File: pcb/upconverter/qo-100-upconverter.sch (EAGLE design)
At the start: 222 parts, among them CON1 3P-SH-SIDE, CON2 2EDG-2P-5MM-H, U1 EFM32TG11B120F128GM32, U10 LTC5597, U11 2450BP15E0100, U12 DC2337J5010AHF, U13 MCP6V31, U14 SKY66292-11, U15 F1958NBGK, U16 MCP9802-A0, U17 MCP1700-330, U18 LT8636, U19 MCP3421-A0, U2 DSB321SDA, U20 MCP6C02-020, U21 ADP7142AUJZ-3.3, U22 ADP7142AUJZ-3.3, U23 ADP7142AUJZ-3.3, U24 ADM7171ACPZ-5.0, U25 ADM7172ACPZ-5.0, U3 ADF4351, U4 F1958NBGK, U5 MAX2671, U6 2450BP15E0100, U7 F1958NBGK, U8 ADL5601, U9 F1490NLGA

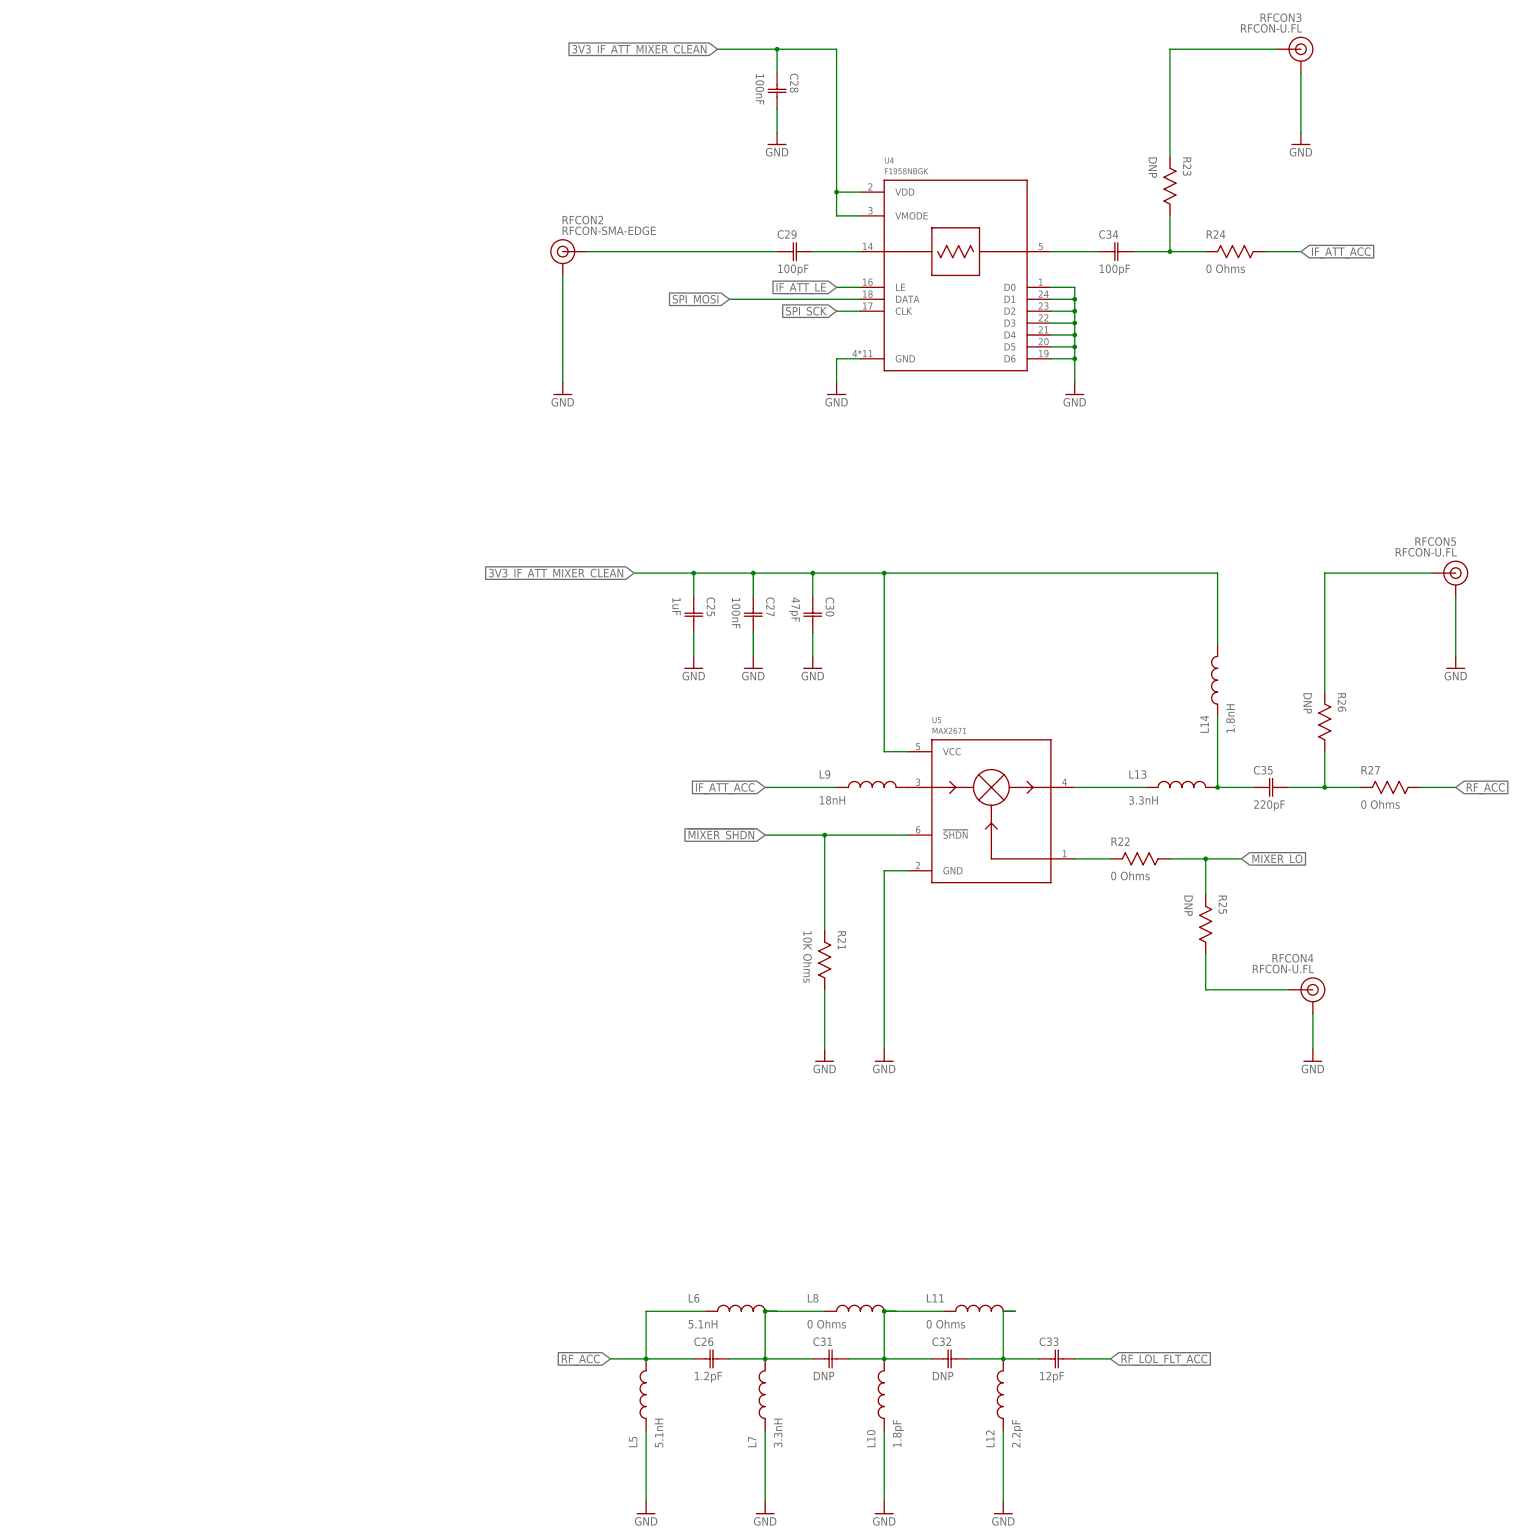
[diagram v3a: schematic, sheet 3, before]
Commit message: Add RF switch
Signed-off-by: João Silva <jgc3silva@gmail.com>
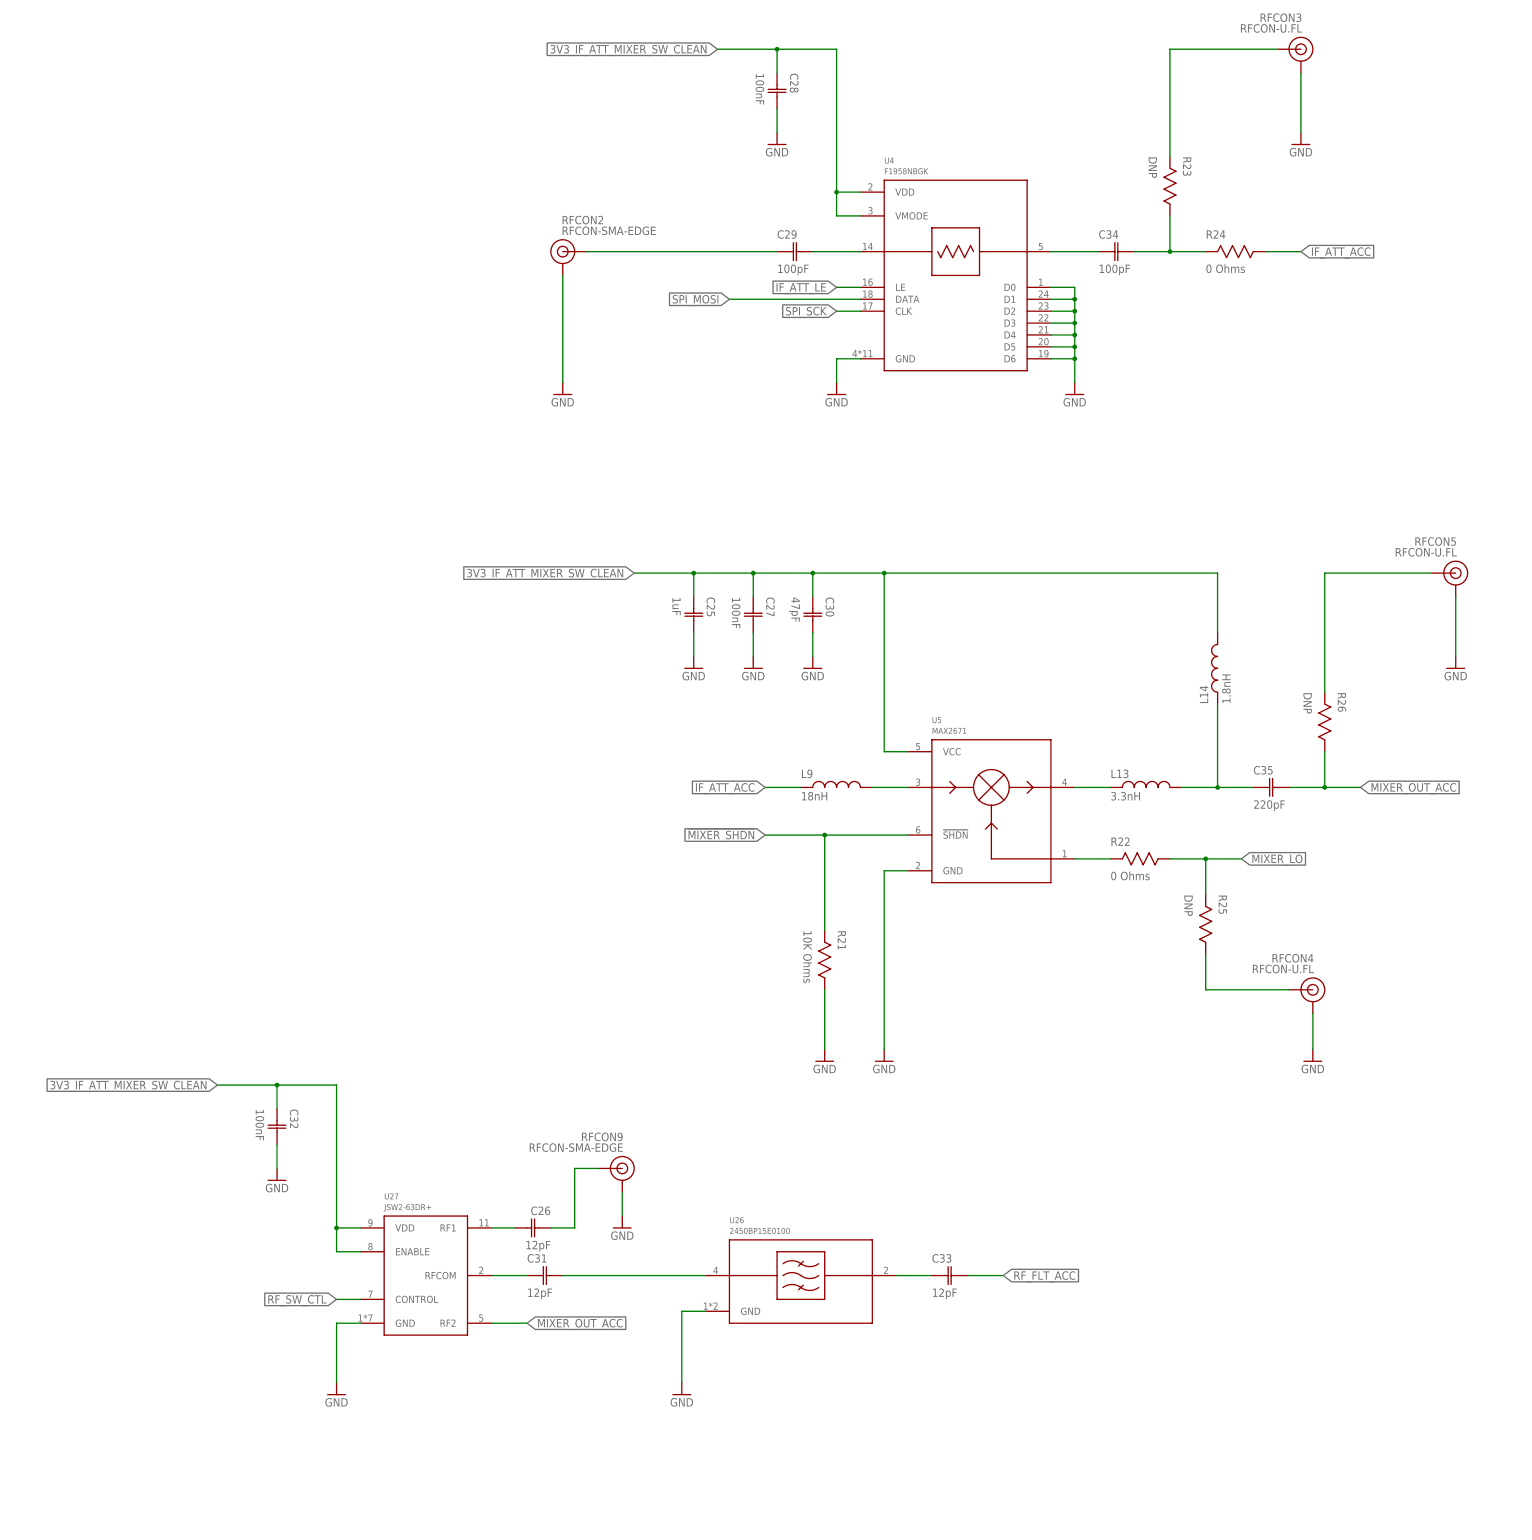
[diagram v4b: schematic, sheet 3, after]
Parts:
- removed L10: 1.8pF, Inductor:INDUCTOR-0603
- removed L11, L8: 0 Ohms, Inductor:INDUCTOR-0603
- removed L12: 2.2pF, Inductor:INDUCTOR-0603
- removed L5, L6: 5.1nH, Inductor:INDUCTOR-0603
- removed L7: 3.3nH, Inductor:INDUCTOR-0603
- removed R27: 0 Ohms, Resistor:RESISTOR-0603
- added RFCON9: RFCON-SMA-EDGE, RF Connector:RFCON-SMA-EDGE
- added U26: 2450BP15E0100, Generic Filter:2450BP15E0100
- added U27: JSW2-63DR+, Mini Circuits:JSW2-63DR+
- C26: value 1.2pF -> 12pF
- C31: value DNP -> 12pF
- C32: value DNP -> 100nF
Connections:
- net RF_LOL_FLT_ACC renamed RF_FLT_ACC
- removed net 3V3_IF_ATT_MIXER_CLEAN: C25.C1, C27.C1, C28.C1, C30.C1, C93.C1, L14.2, U21.SENSE/ADJ, U21.VOUT, U4.VDD, U4.VMODE, U5.VCC
- removed net MIXER_OUT_ACC_PROBE: C35.C2, R26.1, R27.2
- removed net N$32: C26.C2, C31.C1, L6.2, L7.2, L8.1
- removed net N$33: C31.C2, C32.C1, L10.2, L11.1, L8.2
- removed net N$34: C32.C2, C33.C1, L11.2, L12.2
- removed net RF_ACC: C26.C1, L5.2, L6.1, R27.1
- new net 3V3_IF_ATT_MIXER_SW_CLEAN: C25.C1, C27.C1, C28.C1, C30.C1, C32.C1, C93.C1, L14.2, U21.SENSE/ADJ, U21.VOUT, U27.ENABLE, U27.VDD, U4.VDD, U4.VMODE, U5.VCC
- new net MIXER_OUT_ACC: C35.C2, R26.1, U27.RF2
- new net RF_IN_ACC: C26.C2, U27.RF1
- new net RF_IN_DCC: C26.C1, RFCON9.SIGNAL
- new net RF_SEL_ACC: C31.C2, U26.RFIN
- new net RF_SEL_DCC: C31.C1, U27.RFCOM
- new net RF_SEL_FILT_DCC: C33.C1, U26.RFOUT
- new net RF_SW_CTL: U1.PC13, U27.CONTROL
- net GND: now also C32.C2, RFCON9.GND, U26.GND, U27.GND; no longer L10.1, L12.1, L5.1, L7.1
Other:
- moved on the sheet: C26, C31, C32, C33, L1, L13, L14, L15, L17, L2, L3, L4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

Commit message: Add Mixer and RF Switch indicator LEDs Slightly raise switched 5V0 rail voltage to account for larger current drawn from higher power last stage Remove dedicated ADC for current sampling Added PCB preview pictures Added schematic PDF
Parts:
- removed C81: 100nF, Capacitor:CAPACITOR-0603
- removed L16: 470nH, Inductor:INDUCTOR-0603
- removed R10: 100K Ohms, Resistor:RESISTOR-0603
- removed R52: 221K Ohms, Resistor:RESISTOR-0603
- removed RFCON9: RFCON-SMA-EDGE, RF Connector:RFCON-SMA-EDGE
- removed U21: ADP7142AUJZ-3.3, Analog Devices:ADP7142AUJZ-3.3
- added D7, D8: LED0603, LED:LED0603
- added L5: 18nH, Inductor:INDUCTOR-0603
- added R27: 1K Ohms, Resistor:RESISTOR-0603
- C25: value 1uF -> 100nF
- C26, C33: value 12pF -> 15pF
- C27: value 100nF -> 15pF
- C28: value 100nF -> 1uF
- C29: value 100pF -> 100nF
- C30: value 47pF -> 100nF
- C31: value 12pF -> 100pF
- C32: value 100nF -> 47pF
- C65: value 10nF -> 100nF
- C66, C77: value 100nF -> 10nF
- C67: value 15pF -> 100nF
- C68: value 4.7uF -> 15pF; VOLTAGE 35V -> (none)
- C69: value 100nF -> 4.7uF; VOLTAGE (none) -> 35V
- C70: value 470pF -> 100nF
- C72: value 4.7uF -> 470pF
- C73: value 1uF -> 4.7uF; VOLTAGE 50V -> (none)
- C75: VOLTAGE (none) -> 50V
- C76: value 10nF -> 1uF
- C78: value 10uF -> 100nF
- C80: value 100nF -> 10uF
- C82: value 10pF -> 100nF
- C83: value 1uF -> 10pF
- C84: value 100uF -> 1uF; device Capacitor:CAPACITOR-1206 -> Capacitor:CAPACITOR-0603
- C85: value 100nF -> 100uF; device Capacitor:CAPACITOR-0603 -> Capacitor:CAPACITOR-1206
- C87: value 22uF -> 100nF; device Capacitor:CAPACITOR-1206 -> Capacitor:CAPACITOR-0603
- C88: value 1uF -> 22uF; device Capacitor:CAPACITOR-0603 -> Capacitor:CAPACITOR-1206
- C93: value 10uF -> 1uF
- C96: value 1nF -> 10uF
- C98: value 10uF -> 1nF; device Capacitor:CAPACITOR-1206 -> Capacitor:CAPACITOR-0603; VOLTAGE 50V -> (none)
- C99: value 100nF -> 10uF; device Capacitor:CAPACITOR-0603 -> Capacitor:CAPACITOR-1206; VOLTAGE (none) -> 50V
- L9: value 18nH -> 470nH
- R28: value 1K Ohms -> DNP
- R30: value DNP -> 1.5K Ohms
- R31: value 1.5K Ohms -> 0 Ohms
- R32: value 0 Ohms -> 510 Ohms
- R33: value 510 Ohms -> 0 Ohms
- R34: value 0 Ohms -> 1K Ohms
- R35: value DNP -> 2K Ohms
- R36: value 1K Ohms -> 49.9 Ohms
- R37: value 2K Ohms -> 100 Ohms
- R38: value 49.9 Ohms -> 96.1 Ohms
- R39: value 100 Ohms -> 71.5 Ohms
- R41: value 71.5 Ohms -> 10K Ohms
- R42: value 96.1 Ohms -> 7.5K Ohms
- R43: value 10K Ohms -> 510 Ohms
- R44: value 7.5K Ohms -> 100K Ohms
- R45: value 510 Ohms -> 10K Ohms
- R47: value 10K Ohms -> 75K Ohms
- R48: value 100K Ohms -> 41.2K Ohms
- R49: value 75K Ohms -> 1M Ohms
- R50: value 41.2K Ohms -> 220K Ohms
- R51: value 1M Ohms -> 1K Ohms
- R53: value 10K Ohms -> 0.03 Ohms; device Resistor:RESISTOR-0603 -> Resistor:RESISTOR-1206; TOLERANCE (none) -> 1%
- R54: value 10K Ohms -> 100K Ohms
- R55: value 0.03 Ohms -> 100K Ohms; device Resistor:RESISTOR-1206 -> Resistor:RESISTOR-0603; TOLERANCE 1% -> (none)
- R56: value 100K Ohms -> 1K Ohms
- R57: value 100K Ohms -> 330 Ohms
- R58: value 1K Ohms -> 330 Ohms
- RFCON3: value RFCON-U.FL -> RFCON-SMA-EDGE; device RF Connector:RFCON-U.FL -> RF Connector:RFCON-SMA-EDGE
- U10: value LTC5597 -> ADL5601; device Analog Devices:LTC5597 -> Analog Devices:ADL5601
- U11: value 2450BP15E0100 -> F1490NLGA; device Generic Filter:2450BP15E0100 -> Renesas:F1490NLGA
- U12: value DC2337J5010AHF -> LTC5597; device Anaren:DC2337J5010AHF -> Analog Devices:LTC5597; OCLCSC C509396 -> (none)
- U13: value MCP6V31 -> 2450BP15E0100; device Microchip:MCP6V31 -> Generic Filter:2450BP15E0100
- U14: value SKY66292-11 -> DC2337J5010AHF; device Skyworks:SKY66292-11 -> Anaren:DC2337J5010AHF; OCLCSC (none) -> C509396
- U15: value F1958NBGK -> MCP6V31; device Renesas:F1958NBGK -> Microchip:MCP6V31
- U17: value MCP1700-330 -> SKY66292-11; device Microchip:MCP1700-330 -> Skyworks:SKY66292-11
- U18: value LT8636 -> F1958NBGK; device Analog Devices:LT8636 -> Renesas:F1958NBGK
- U19: value MCP3421-A0 -> MCP1700-330; device Microchip:MCP3421-A0 -> Microchip:MCP1700-330
- U20: value MCP6C02-020 -> LT8636; device Microchip:MCP6C02-020 -> Analog Devices:LT8636
- U22: value ADP7142AUJZ-3.3 -> MCP6C02-020; device Analog Devices:ADP7142AUJZ-3.3 -> Microchip:MCP6C02-020
- U24: value ADM7171ACPZ-5.0 -> ADP7142AUJZ-3.3; device Analog Devices:ADM7171ACPZ-5.0 -> Analog Devices:ADP7142AUJZ-3.3
- U25: value ADM7172ACPZ-5.0 -> ADP7142AUJZ-3.3; device Analog Devices:ADM7172ACPZ-5.0 -> Analog Devices:ADP7142AUJZ-3.3
- U26: value 2450BP15E0100 -> ADM7171ACPZ-5.0; device Generic Filter:2450BP15E0100 -> Analog Devices:ADM7171ACPZ-5.0
- U27: value JSW2-63DR+ -> ADM7172ACPZ-5.0; device Mini Circuits:JSW2-63DR+ -> Analog Devices:ADM7172ACPZ-5.0
- U4: value F1958NBGK -> JSW2-63DR+; device Renesas:F1958NBGK -> Mini Circuits:JSW2-63DR+
- U5: value MAX2671 -> 2450BP15E0100; device Maxim Integrated:MAX2671 -> Generic Filter:2450BP15E0100
- U6: value 2450BP15E0100 -> F1958NBGK; device Generic Filter:2450BP15E0100 -> Renesas:F1958NBGK
- U7: value F1958NBGK -> MAX2671; device Renesas:F1958NBGK -> Maxim Integrated:MAX2671
- U8: value ADL5601 -> 2450BP15E0100; device Analog Devices:ADL5601 -> Generic Filter:2450BP15E0100
- U9: value F1490NLGA -> F1958NBGK; device Renesas:F1490NLGA -> Renesas:F1958NBGK
- renumbered L13 to L6, L14 to L7, L15 to L8, L17 to L10, L18 to L11, L19 to L12
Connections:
- removed net !PLL_MUTE: R10.2, U1.PE13, U3.!PDRF
- removed net 5V0_ISENSE_VN: C85.C2, R54.1, U19.VIN-
- removed net 5V0_ISENSE_VP: C85.C1, R53.1, U19.VIN+
- removed net N$10: R53.2, U20.VOUT
- removed net N$48: R35.2, RFCON7.SIGNAL
- new net N$5: D7.A, R57.1
- new net N$9: D8.A, R58.1
- new net V5V0_ISENSE: C86.C1, R51.1, U1.PE13
- new net V5V0_ISENSE-AMP: R51.2, U22.VOUT
- net !MIXER_SHDN: now also R57.2, U7.!SHDN; no longer U5.!SHDN
- net 3V3: now also C65.C1, U19.VOUT; no longer C77.C1, C99.C1, U17.VOUT, U19.VDD
- net 3V3_IF_ATT_MIXER_SW_CLEAN: now also C29.C1, C94.C1, U23.SENSE/ADJ, U23.VOUT, U4.ENABLE, U6.VDD, U6.VMODE, U7.VCC; no longer C27.C1, C93.C1, U21.SENSE/ADJ, U21.VOUT, U27.ENABLE, U27.VDD, U4.VMODE, U5.VCC
- net 3V3_PLL_CLEAN: now also C96.C1, U25.SENSE/ADJ, U25.VOUT; no longer C95.C1, U23.SENSE/ADJ, U23.VOUT
- net 3V3_RF_ATT_PDET_CLEAN: now also C67.C1, C95.C1, U12.EN, U12.VCC, U15.PWR.V+, U18.VDD, U18.VMODE, U24.SENSE/ADJ, U24.VOUT, U9.VDD, U9.VMODE; no longer C66.C1, C94.C1, U10.EN, U10.VCC, U13.PWR.V+, U15.VDD, U15.VMODE, U22.SENSE/ADJ, U22.VOUT, U7.VDD, U7.VMODE
- net 5V0: now also C70.C1, C73.C1, C85.C1, C87.C1, R46.2, R49.2, R53.2, R56.2, U19.VIN, U20.BIAS, U22.VDD, U22.VIP; no longer C69.C1, C72.C1, C82.C1, C86.C1, R48.2, R51.2, R55.2, R58.2, U17.VIN, U18.BIAS, U20.VDD, U20.VIP
- net 5V0_BST: now also C82.C2, U20.BST; no longer C81.C2, U18.BST
- net 5V0_FB: now also C83.C2, R49.1, R50.2, U20.FB; no longer C82.C2, R51.1, R52.2, U18.FB
- net 5V0_INTVCC: now also C76.C1, U20.INTVCC, U20.SYNC/MODE; no longer C75.C1, U18.INTVCC, U18.SYNC/MODE
- net 5V0_ISENSE: now also C93.C1, R53.1, U22.VIM, U24.EN, U25.EN, U26.VIN, U27.VIN; no longer C87.C1, R55.1, U20.VIM, U21.EN, U21.VIN, U22.EN, U22.VIN
- net 5V0_PA_STG1_2_CLEAN: now also L9.2, R27.2, R30.2, R32.2, U26.SENSE, U26.VOUT; no longer L16.2, R29.2, R31.2, R33.2, U24.SENSE, U24.VOUT
- net 5V0_PA_STG3_CLEAN: now also C66.C1, R41.2, U17.VBIAS, U17.VCC, U27.SENSE, U27.VOUT; no longer C65.C1, R45.2, U14.VBIAS, U14.VCC, U25.SENSE, U25.VOUT
- net 5V0_RT: now also R48.2, U20.RT; no longer R50.2, U18.RT
- net 5V0_SS: now also C77.C1, U20.TR/SS; no longer C76.C1, U18.TR/SS
- net 5V0_SW: now also C82.C1, U20.SW; no longer C81.C1, U18.SW
- net 5V0_VSENSE: now also C72.C1, R46.1, R47.2; no longer C71.C1, R48.1, R49.2
- net GND: now also C29.C2, C67.C2, C85.C2, D7.C, D8.C, R34.1, R45.1, R48.1, R54.1, R55.1, U12.GND@0, U12.GND@1, U12.GND@2, U12.GND@3, U13.GND, U15.PWR.V-, U18.D0, U18.D1, U18.D2, U18.D3, U18.D4, U18.D5, U18.D6, U19.GND, U20.GND, U22.VREF, U22.VSS, U6.D0, U6.D1, U6.D2, U6.D3, U6.D4, U6.D5, U6.D6, U8.GND, U9.D0, U9.D1, U9.D2, U9.D3, U9.D4, U9.D5, U9.D6; no longer C27.C2, C68.C2, C83.C2, R10.1, R44.1, R49.1, R52.1, R54.2, R56.1, R57.1, RFCON9.GND, U10.GND@2, U10.GND@3, U12.GND, U13.PWR.V-, U15.D0, U15.D1, U15.D2, U15.D3, U15.D4, U15.D5, U15.D6, U15.GND, U19.VSS, U20.VREF, U20.VSS, U21.GND, U22.GND, U4.D0, U4.D1, U4.D2, U4.D3, U4.D4, U4.D5, U4.D6, U7.D0, U7.D1, U7.D2, U7.D3, U7.D4, U7.D5, U7.D6, U8.GND@0, U8.GND@1
- net I2C1_SCL: no longer U19.SCL
- net I2C1_SDA: no longer U19.SDA
- net IF_ATT_ACC: now also L5.1; no longer L9.1
- net IF_ATT_DCC: now also U6.RF1; no longer U4.RF1
- net IF_ATT_LE: now also U6.LE; no longer U4.LE
- net IF_IN_ACC: now also C31.C2, U6.RF2; no longer C29.C2, U4.RF2
- net IF_IN_DCC: now also C31.C1; no longer C29.C1
- net MIXER_IN_DCC: now also L5.2, U7.IFIN; no longer L9.2, U5.IFIN
- net MIXER_OUT_ACC: now also U4.RF2; no longer U27.RF2
- net MIXER_OUT_DCC: now also U7.RFOUT; no longer U5.RFOUT
- net N$12: now also U11.VDD; no longer U9.VDD
- net N$149: now also R56.1; no longer R58.1
- net N$15: now also R27.1, U11.BIAS1; no longer R28.1, U9.BIAS1
- net N$16: now also R30.1, U11.BIAS2; no longer R31.1, U9.BIAS2
- net N$2: now also C98.C1, U27.SS; no longer C97.C1, U25.SS
- net N$20: now also C97.C1, U26.SS; no longer C96.C1, U24.SS
- net N$23: now also R32.1; no longer R33.1
- net N$24: now also RFCON4.SIGNAL; no longer RFCON3.SIGNAL
- net N$28: now also RFCON6.SIGNAL; no longer RFCON5.SIGNAL
- net N$3: now also R43.1; no longer R45.1
- net N$30: now also U11.RFIN; no longer U9.RFIN
- net N$35: now also R29.2, RFCON7.SIGNAL; no longer R30.2, RFCON6.SIGNAL
- net N$39: now also U18.RF2; no longer U15.RF2
- net N$4: now also R28.1, U11.GAIN_SEL; no longer R29.1, U9.GAIN_SEL
- net N$42: now also R36.2, U14.ISOLATED; no longer R38.2, U12.ISOLATED
- net N$43: now also U12.RFIN; no longer U10.RFIN
- net N$44: now also U12.FLTR; no longer U10.FLTR
- net N$45: now also U7.LO; no longer U5.LO
- net N$47: now also RFCON5.SIGNAL; no longer RFCON4.SIGNAL
- net N$7: now also R34.2, R35.2, U15.1.-IN; no longer R36.2, R37.2, U13.1.-IN
- net N$8: now also U3.!PDRF
- net PA3_EN: now also R41.1, R42.2, U17.PAEN; no longer R43.1, R44.2, U14.PAEN
- net PA_STG1_2_BIAS_EN: now also R54.2, U26.EN; no longer R56.2, U24.EN
- net PA_STG3_BIAS_EN: now also R55.2, U27.EN; no longer R57.2, U25.EN
- net RF_ATT1_LE: now also U9.LE; no longer U7.LE
- net RF_ATT2_LE: now also U18.LE; no longer U15.LE
- net RF_FINAL_ACC: now also U17.RFOUT; no longer U14.RFOUT
- net RF_FLT_ACC: now also U10.RFIN; no longer U8.RFIN
- net RF_IN_ACC: now also C27.C2, U4.RF1; no longer C26.C2, U27.RF1
- net RF_IN_DCC: now also C27.C1, RFCON3.SIGNAL; no longer C26.C1, RFCON9.SIGNAL
- net RF_PRE1_ACC: now also U9.RF2; no longer U7.RF2
- net RF_PRE1_ATT_ACC: now also R31.1, U8.RFIN; no longer R32.1, U6.RFIN
- net RF_PRE1_ATT_ACC_PROBE: now also R29.1, R31.2; no longer R30.1, R32.2
- net RF_PRE1_ATT_DCC: now also U9.RF1; no longer U7.RF1
- net RF_PRE1_ATT_FLT_ACC: now also U8.RFOUT; no longer U6.RFOUT
- net RF_PRE1_DCC: now also L9.1, U10.RFOUT; no longer L16.1, U8.RFOUT
- net RF_PRE2_ATT_ACC: now also C68.C2, U13.RFIN; no longer C67.C2, U11.RFIN
- net RF_PRE2_ATT_DCC: now also C68.C1, U18.RF1; no longer C67.C1, U15.RF1
- net RF_PRE2_ATT_FLT_ACC: now also U13.RFOUT, U14.IN; no longer U11.RFOUT, U12.IN
- net RF_PRE2_ATT_FLT_CPL_ACC: now also U14.COUPLED; no longer R35.1, U12.COUPLED
- net RF_PRE2_ATT_FLT_THRU_ACC: now also R38.2, R39.2, U14.OUT; no longer R40.2, R41.2, U12.OUT
- net RF_PRE2_ATT_FLT_THRU_ACC_ATT: now also R39.1, R40.2, U17.RFIN; no longer R41.1, R42.2, U14.RFIN
- net RF_PRE2_DCC: now also U11.RFOUT; no longer U9.RFOUT
- net RF_SEL_ACC: now also C26.C2, U5.RFIN; no longer C31.C2, U26.RFIN
- net RF_SEL_DCC: now also C26.C1, U4.RFCOM; no longer C31.C1, U27.RFCOM
- net RF_SEL_FILT_DCC: now also U5.RFOUT; no longer U26.RFOUT
- net RF_SW_CTL: now also R58.2, U4.CONTROL; no longer U27.CONTROL
- net SPI_MOSI: now also U18.DATA, U6.DATA, U9.DATA; no longer U15.DATA, U4.DATA, U7.DATA
- net SPI_SCK: now also U18.CLK, U6.CLK, U9.CLK; no longer U15.CLK, U4.CLK, U7.CLK
- net VIN: now also C69.C1, C75.C1, C99.C1, R44.2, U20.EN/UV, U20.VIN; no longer C68.C1, C73.C1, C98.C1, R46.2, U18.EN/UV, U18.VIN
- net VIN_VSENSE: now also C71.C1, R44.1, R45.2; no longer C70.C1, R46.1, R47.2
- net VPDET_AMP: now also R35.1, R37.2, U15.1.OUT; no longer R37.1, R39.2, U13.1.OUT
- net VPDET_FLT: now also R33.1, U15.1.+IN; no longer R34.1, U13.1.+IN
- net VPDET_RAW: now also R33.2, U12.OUT; no longer R34.2, U10.OUT
- net VPDET_SENSE: now also R37.1; no longer R39.1
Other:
- note added: "+35.5 dB"
- note removed: "+39.5 dB"
- moved on the sheet: C25, C26, C27, C28, C29, C30, C31, C32, C65, C66, C67, C69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
